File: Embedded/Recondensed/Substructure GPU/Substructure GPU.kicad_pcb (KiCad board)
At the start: 4 copper layers, 60 x 35 mm, 38 parts, among them J1 10171746-00021LF, J11 Substructure Power, J13 MicroSD, J2 HUB75 Right, J3 Display Power, J4 HUB75 Left, J5 Expansion Data, J6 Expansion PWR, SW2 RST, U2 74HC245D_653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

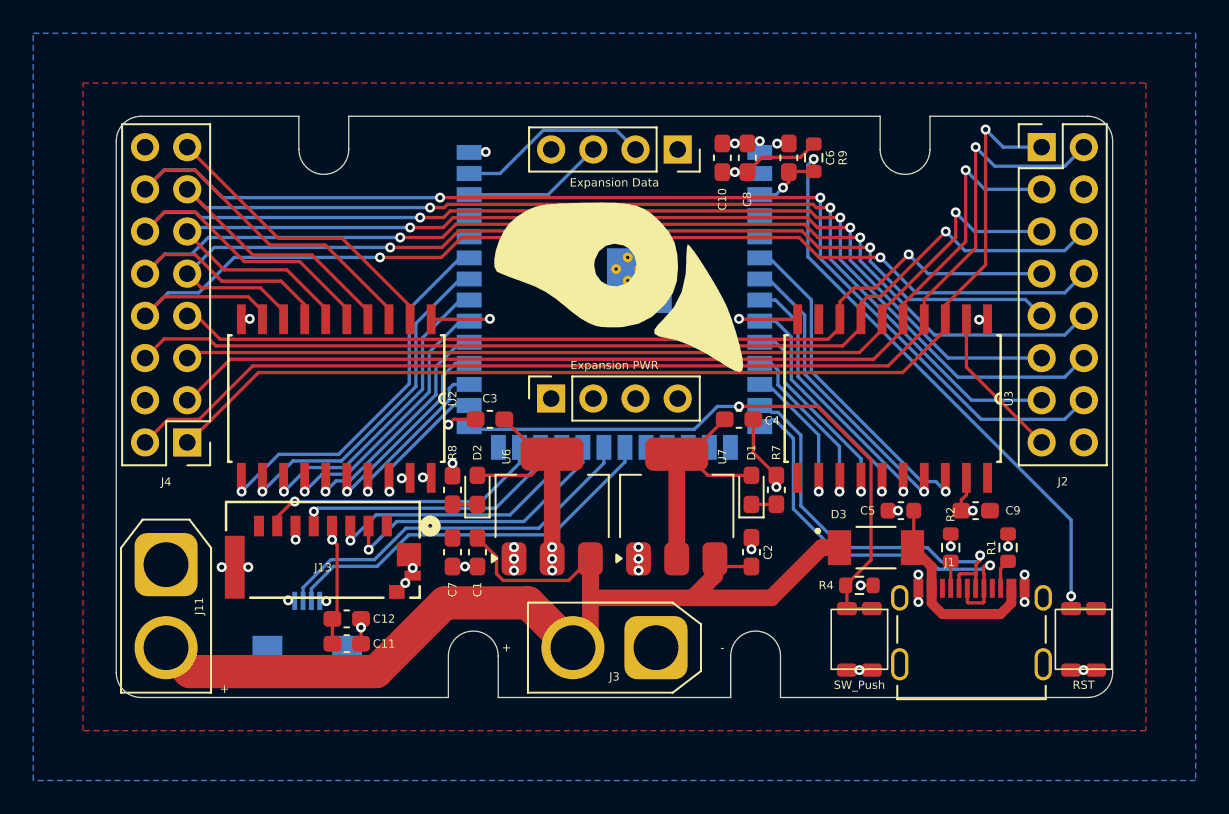
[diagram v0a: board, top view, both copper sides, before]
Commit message: Added LCSC Component IDs
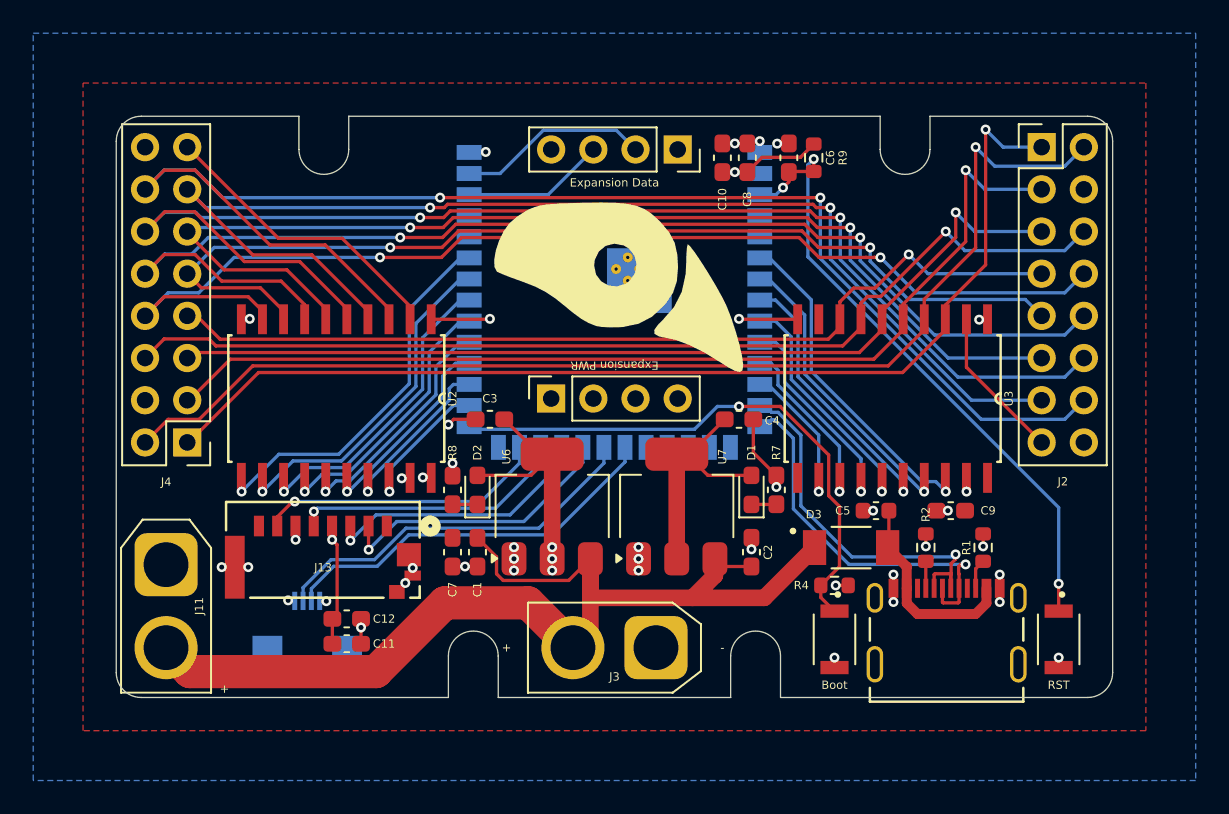
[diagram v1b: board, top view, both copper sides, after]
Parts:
- removed BootSW1: SW_Push, Buttons:R-667843
- removed SW2: RST, Buttons:R-667843
- added S1: Boot, Buttons:SW_B3U-1000P, F.Cu at (108.2, 71.5)
- added S2: RST, Buttons:SW_B3U-1000P, F.Cu at (121.8, 71.5)
- J1: footprint USBC:AMPHENOL_10171746-00021LF -> USBC:MOLEX_2171790001
- R7: value 155ohm min -> 147ohm
- R8: value 70ohm min -> 33ohm
- moved J1 1.89 mm to (115.0, 71.8)
- moved C5 1.50 mm to (110.8, 63.8)
- moved C9 1.50 mm to (115.2, 63.8)
- moved D3 1.50 mm to (109.2, 66.0)
- moved R1 1.50 mm to (117.2, 66.0)
- moved R2 1.50 mm to (113.8, 66.0)
- moved R4 1.50 mm to (108.2, 68.2)
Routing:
- net Net-(ESP1-GPIO0/BOOT): track 37.3 -> 34.1 mm
- net GND: track 43.2 -> 40.1 mm, vias 38 -> 39
- net Main USB -: track 24.8 -> 23.0 mm
- net Net-(ESP1-EN): track 40.2 -> 38.5 mm
- net Main USB +: track 24.8 -> 23.1 mm
- net +RAWVS: track 159.8 -> 158.3 mm

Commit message: Updated Asset Dates
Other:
- board text added: "Des: CSF-Substructure-GPU M/N: CSF-AAA-000 Rev: D0.0 Dat: 27.07.2025"
- board text removed: "Des: CSF-Substructure-GPU M/N: CSF-AAA-000 Rev: D0.0 Dat: 26.07.2025"
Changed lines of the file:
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@@
 		)
 	)
-	(gr_text "Des: CSF-Substructure-GPU\nM/N: CSF-AAA-000\nRev: D0.0\nDat: 26.07.2025"
+	(gr_text "Des: CSF-Substructure-GPU\nM/N: CSF-AAA-000\nRev: D0.0\nDat: 27.07.2025"
 		(at 100.5 63.25 0)
 		(layer "B.SilkS")

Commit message: Modified Tables per component to centralise LCSC IDs
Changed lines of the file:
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@@
 				(font
 					(size 0.5 0.5)
-					(thickness 0.15)
+					(thickness 0.125)
 				)
 			)
@@
 				(font
 					(size 0.5 0.5)
-					(thickness 0.15)
+					(thickness 0.125)
 				)
 			)
@@
 				(font
 					(size 0.5 0.5)
-					(thickness 0.15)
+					(thickness 0.125)
 				)
 			)
@@
 				(font
 					(size 0.5 0.5)
-					(thickness 0.15)
+					(thickness 0.125)
 				)
 			)
@@
 		(sheetname "/")
 		(sheetfile "Substructure GPU.kicad_sch")
-		(attr through_hole)
+		(attr through_hole exclude_from_pos_files exclude_from_bom)
 		(fp_line
 			(start -1.01 2.71)
@@
 				(font
 					(size 0.5 0.5)
-					(thickness 0.15)
+					(thickness 0.125)
 				)
 			)
@@
 				(font
 					(size 0.5 0.5)
-					(thickness 0.15)
+					(thickness 0.125)
 				)
 			)
@@
 				(font
 					(size 0.5 0.5)
-					(thickness 0.15)
+					(thickness 0.125)
 				)
 			)
@@
 				(font
 					(size 0.5 0.5)
-					(thickness 0.15)
+					(thickness 0.125)
 				)
 			)
@@
 		(sheetname "/")
 		(sheetfile "Substructure GPU.kicad_sch")
-		(attr through_hole)
+		(attr through_hole exclude_from_pos_files exclude_from_bom)
 		(fp_line
 			(start 7.71 -2.71)
@@
 		(sheetname "/")
 		(sheetfile "Substructure GPU.kicad_sch")
-		(attr through_hole)
+		(attr through_hole exclude_from_pos_files exclude_from_bom)
 		(fp_line
 			(start 1.33 -1.33)
@@
 		(tags "Through hole socket strip THT 1x04 2.54mm single row")
 		(property "Reference" "J5"
-			(at 0 -2.77 270)
+			(at 0 -2.77 90)
 			(layer "F.Fab")
 			(hide yes)
@@
 		)
 		(property "Datasheet" ""
-			(at 0 0 270)
+			(at 0 0 90)
 			(layer "F.Fab")
 			(hide yes)
@@
 		)
 		(property "Description" "Generic connector, single row, 01x04, script generated (kicad-library-utils/schlib/autogen/connector/)"
-			(at 0 0 270)
+			(at 0 0 90)
 			(layer "F.Fab")
 			(hide yes)
@@
 		(sheetname "/")
 		(sheetfile "Substructure GPU.kicad_sch")
-		(attr through_hole)
+		(attr through_hole exclude_from_pos_files exclude_from_bom)
 		(fp_line
 			(start -1.33 8.95)
@@
 		(sheetname "/")
 		(sheetfile "Substructure GPU.kicad_sch")
-		(attr smd)
+		(attr smd exclude_from_pos_files exclude_from_bom)
 		(fp_line
 			(start 9.2 9.8)
@@
 		(sheetname "/")
 		(sheetfile "Substructure GPU.kicad_sch")
-		(attr smd)
+		(attr smd exclude_from_pos_files exclude_from_bom)
 		(fp_line
 			(start 3.5 -0.1)

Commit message: Added Pullups for MicroSD & Modified Silkscreen
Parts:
- added R10: 10K, Resistor_SMD:R_0603_1608Metric, F.Cu at (70.5, 62.2)
- added R11: 10K, Resistor_SMD:R_0603_1608Metric, F.Cu at (79.1, 70.1)
- added R12: 10K, Resistor_SMD:R_0603_1608Metric, F.Cu at (67.5, 63.1)
- added R3: 10K, Resistor_SMD:R_0603_1608Metric, F.Cu at (79.1, 71.6)
- added R5: 10K, Resistor_SMD:R_0603_1608Metric, F.Cu at (76.1, 70.1)
- added R6: 10K, Resistor_SMD:R_0603_1608Metric, F.Cu at (76.1, 71.6)
- moved C11 5.98 mm to (72.9, 71.6), turned to 180 degrees
- moved C12 5.98 mm to (72.9, 70.1), turned to 180 degrees
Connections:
- J13 pad 1: unconnected-(J13-Pad1) -> Net-(J13-Pad1)
- J13 pad 8: unconnected-(J13-Pad8) -> Net-(J13-Pad8)
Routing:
- net SD SPI CLK: track 16.7 -> 24.4 mm
- net SD SPI CS: track 17.4 -> 23.6 mm
- net Net-(J13-Pad1): track 0.00 -> 5.99 mm
- net Net-(J13-Pad8): track 0.00 -> 5.92 mm
- net SD SPI MOSI: track 16.5 -> 21.9 mm
- net SD SPI MISO: track 17.4 -> 22.5 mm
- net GND: track 40.1 -> 43.6 mm, vias 39 -> 38
- net +3V3: track 31.4 -> 32.0 mm, vias 6 -> 11
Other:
- board text added: "Des: CSF-Substructure-GPU M/N: CSF-AAA-000 Rev: D0.0 Dat: 28.07.2025"
- board text removed: "Des: CSF-Substructure-GPU M/N: CSF-AAA-000 Rev: D0.0 Dat: 27.07.2025"
